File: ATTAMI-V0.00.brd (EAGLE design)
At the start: 22.8 x 22.9 mm, 24 parts, among them U1 MIC5225, U2 ATTINY85-20SU

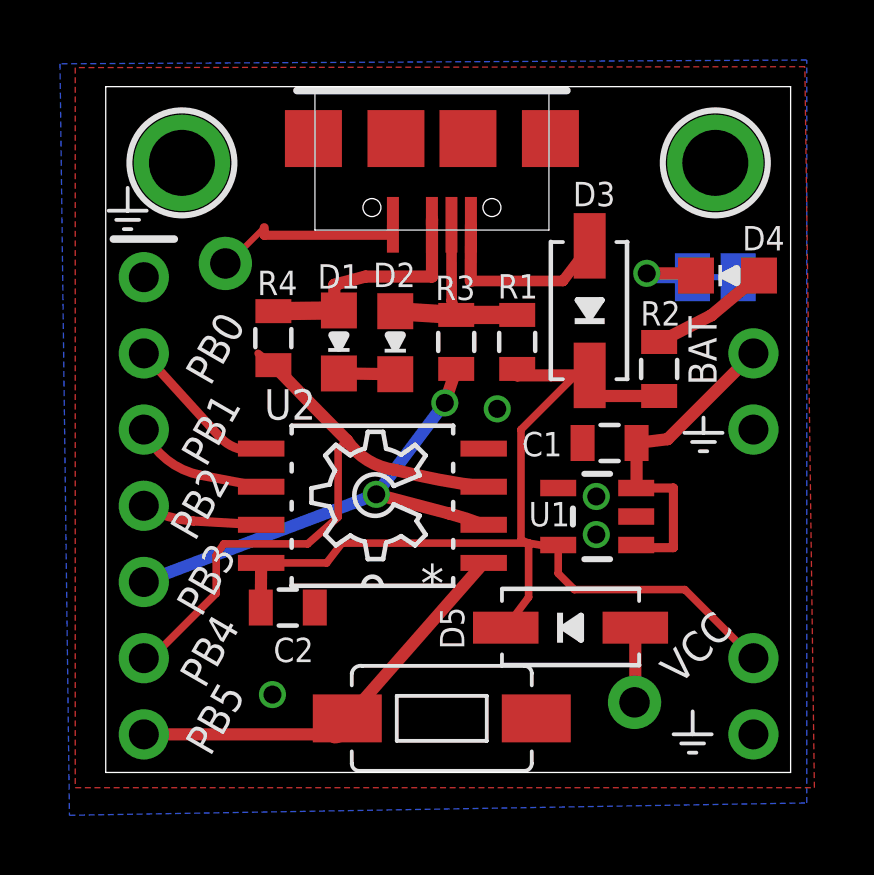
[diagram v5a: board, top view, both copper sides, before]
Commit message: changes in trace width (8mil) and fine tune the aliexpress microusb packge
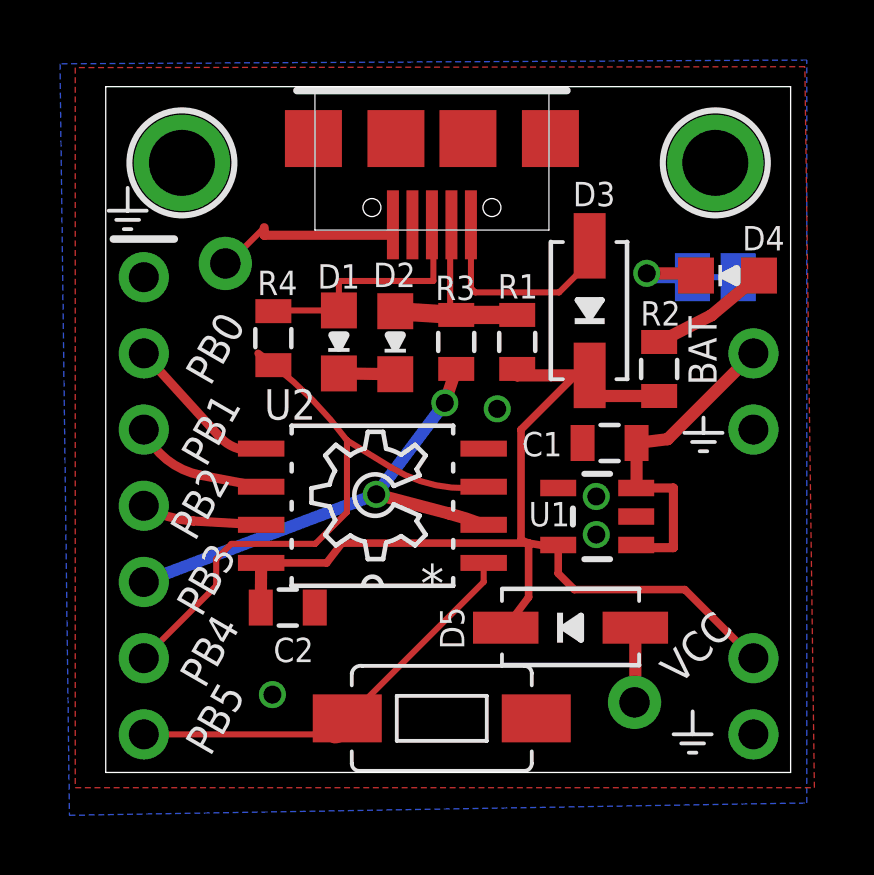
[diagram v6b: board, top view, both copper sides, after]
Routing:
- net V-BUS: track 6.60 -> 7.26 mm
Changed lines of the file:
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@@
 <wire x1="11.684" y1="15.251" x2="13.716" y2="15.251" width="0.6096" layer="1"/>
 <wire x1="11.523740625" y1="18.2553" x2="11.557" y2="18.4553" width="0.3048" layer="1"/>
-<wire x1="11.684" y1="15.251" x2="11.5316" y2="15.7226" width="0.3556" layer="1"/>
-<wire x1="11.5316" y1="15.7226" x2="11.523740625" y2="18.2553" width="0.3556" layer="1"/>
+<wire x1="11.523740625" y1="18.2553" x2="11.4808" y2="18.2553" width="0.2032" layer="1"/>
+<wire x1="11.4808" y1="18.2553" x2="11.4808" y2="15.4542" width="0.2032" layer="1"/>
+<wire x1="11.4808" y1="15.4542" x2="11.684" y2="15.251" width="0.2032" layer="1"/>
 </signal>
 <signal name="GND">
@@
 <contactref element="R4" pad="2"/>
 <wire x1="5.08" y1="13.97" x2="5.588" y2="13.578" width="0.254" layer="1"/>
-<wire x1="8.041640625" y1="11.06931875" x2="5.588" y2="13.578" width="0.4064" layer="1" curve="-1.045178"/>
-<wire x1="8.041640625" y1="11.06931875" x2="9.652" y2="10.0838" width="0.4064" layer="1" curve="48.784139"/>
 <contactref element="J1" pad="6"/>
 <contactref element="U2" pad="3"/>
-<wire x1="9.652" y1="10.0838" x2="12.5984" y2="9.525" width="0.4064" layer="1" curve="7.241306"/>
 <wire x1="1.27" y1="3.81" x2="1.524" y2="3.81" width="0.254" layer="1"/>
-<wire x1="1.524" y1="3.81" x2="3.683" y2="5.969" width="0.254" layer="1"/>
-<wire x1="3.683" y1="5.969" x2="3.683" y2="7.239" width="0.254" layer="1"/>
-<wire x1="3.683" y1="7.239" x2="3.937" y2="7.62" width="0.254" layer="1"/>
-<wire x1="3.937" y1="7.62" x2="6.731" y2="7.62" width="0.254" layer="1"/>
-<wire x1="6.731" y1="7.62" x2="7.747" y2="8.509" width="0.254" layer="1"/>
-<wire x1="7.747" y1="8.509" x2="7.747" y2="10.774678125" width="0.254" layer="1"/>
-<wire x1="7.747" y1="10.774678125" x2="8.041640625" y2="11.06931875" width="0.254" layer="1"/>
+<wire x1="5.588" y1="13.578" x2="8.041640625" y2="11.06931875" width="0.2032" layer="1" curve="-15.959573"/>
+<wire x1="8.041640625" y1="11.06931875" x2="9.525" y2="10.16" width="0.2032" layer="1"/>
+<wire x1="9.525" y1="10.16" x2="12.5984" y2="9.525" width="0.2032" layer="1" curve="39.670268"/>
+<wire x1="8.041640625" y1="11.06931875" x2="8.041640625" y2="8.676640625" width="0.2032" layer="1"/>
+<wire x1="8.041640625" y1="8.676640625" x2="6.985" y2="7.62" width="0.2032" layer="1"/>
+<wire x1="6.985" y1="7.62" x2="4.191" y2="7.62" width="0.2032" layer="1"/>
+<wire x1="4.191" y1="7.62" x2="3.683" y2="7.112" width="0.2032" layer="1"/>
+<wire x1="3.683" y1="7.112" x2="3.683" y2="6.223" width="0.2032" layer="1"/>
+<wire x1="3.683" y1="6.223" x2="1.27" y2="3.81" width="0.2032" layer="1"/>
 </signal>
 <signal name="PB5">
@@
 <wire x1="8.0514" y1="1.8034" x2="7.645" y2="1.27" width="0.6096" layer="1" curve="-90"/>
 <contactref element="J1" pad="7"/>
-<wire x1="1.27" y1="1.27" x2="7.645" y2="1.27" width="0.4064" layer="1"/>
 <contactref element="U2" pad="1"/>
-<wire x1="12.5984" y1="6.985" x2="8.0514" y2="1.8034" width="0.4064" layer="1"/>
+<wire x1="12.5984" y1="6.985" x2="12.5984" y2="6.3504" width="0.2032" layer="1"/>
+<wire x1="12.5984" y1="6.3504" x2="8.0514" y2="1.8034" width="0.2032" layer="1"/>
+<wire x1="7.645" y1="1.27" x2="1.27" y2="1.27" width="0.2032" layer="1"/>
 </signal>
 <signal name="V_BAT">
@@
 <contactref element="D1" pad="A"/>
 <contactref element="USB" pad="DP"/>
-<wire x1="5.588" y1="15.378" x2="7.7724" y2="15.401" width="0.6096" layer="1"/>
-<wire x1="10.873740625" y1="18.2553" x2="10.87628125" y2="18.4553" width="0.4064" layer="1"/>
-<wire x1="10.87628125" y1="18.4553" x2="10.87628125" y2="16.53031875" width="0.4064" layer="1"/>
-<wire x1="10.87628125" y1="16.53031875" x2="8.65631875" y2="16.53031875" width="0.4064" layer="1"/>
-<wire x1="8.65631875" y1="16.53031875" x2="7.62" y2="16.256" width="0.4064" layer="1"/>
-<wire x1="7.62" y1="16.256" x2="7.62" y2="15.5534" width="0.4064" layer="1"/>
-<wire x1="7.62" y1="15.5534" x2="7.7724" y2="15.401" width="0.4064" layer="1"/>
+<wire x1="10.873740625" y1="18.2553" x2="10.922" y2="18.2553" width="0.2032" layer="1"/>
+<wire x1="10.922" y1="18.2553" x2="10.922" y2="16.383" width="0.2032" layer="1"/>
+<wire x1="10.922" y1="16.383" x2="7.7724" y2="16.383" width="0.2032" layer="1"/>
+<wire x1="7.7724" y1="16.383" x2="7.7724" y2="15.401" width="0.2032" layer="1"/>
+<wire x1="7.7724" y1="15.401" x2="5.611" y2="15.401" width="0.2032" layer="1"/>
+<wire x1="5.611" y1="15.401" x2="5.588" y2="15.378" width="0.2032" layer="1"/>
 </signal>
 <signal name="VCC">
@@
 <contactref element="USB" pad="VCC"/>
 <contactref element="D3" pad="AQ"/>
-<wire x1="12.173740625" y1="18.2553" x2="12.1666" y2="16.383" width="0.4064" layer="1"/>
 <wire x1="16.0274" y1="17.7038" x2="16.1315375" y2="17.553940625" width="0.4064" layer="1" curve="-7.449454"/>
-<wire x1="12.1666" y1="16.383" x2="15.24" y2="16.383" width="0.3556" layer="1"/>
-<wire x1="15.24" y1="16.383" x2="16.1315375" y2="17.553940625" width="0.3556" layer="1"/>
+<wire x1="12.173740625" y1="18.2553" x2="12.173740625" y2="16.147259375" width="0.2032" layer="1"/>
+<wire x1="12.173740625" y1="16.147259375" x2="12.319" y2="16.002" width="0.2032" layer="1"/>
+<wire x1="12.319" y1="16.002" x2="15.113" y2="16.002" width="0.2032" layer="1"/>
+<wire x1="15.113" y1="16.002" x2="16.002" y2="16.891" width="0.2032" layer="1"/>
+<wire x1="16.002" y1="16.891" x2="16.002" y2="17.424403125" width="0.2032" layer="1"/>
+<wire x1="16.002" y1="17.424403125" x2="16.1315375" y2="17.553940625" width="0.2032" layer="1"/>
 </signal>
 <signal name="N$2">

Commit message: new design with added AMS1117 voltage regulator
with library reflecting the part
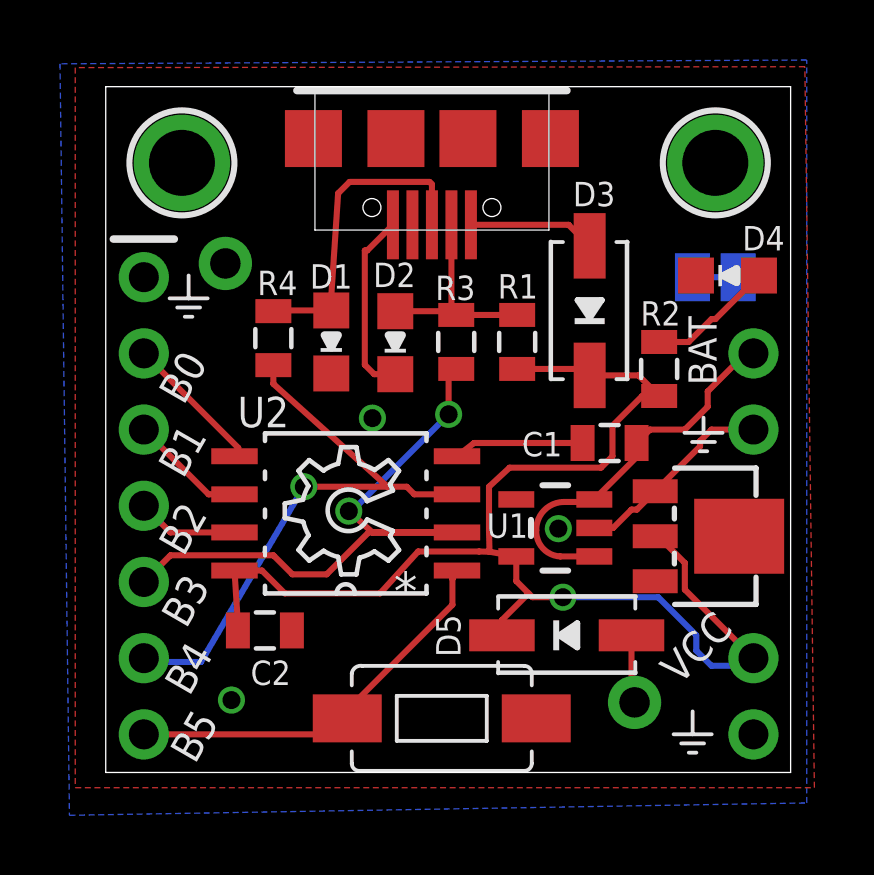
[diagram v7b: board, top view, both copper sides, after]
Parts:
- added 1117: (no value), ATtami:SOT89
- moved U1 1.45 mm to (15.0, 8.15)
- moved C2 1.08 mm to (5.31, 4.73)
- moved U$3 1.02 mm to (9.78, 6.60)
- moved U2 0.92 mm to (8.00, 8.64)
- moved D5 0.28 mm to (15.4, 4.57)
- moved D1 0.25 mm to (7.52, 14.4)
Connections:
- net GND: now also 1117.1
- net VCC: now also 1117.2
- net V_BAT: now also 1117.3
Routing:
- net GND: track 8.55 -> 17.4 mm, vias 4 -> 3
- net VCC: track 36.1 -> 44.7 mm, vias 0 -> 1
- net PB3: track 17.0 -> 21.8 mm
- net N$7: track 8.25 -> 11.5 mm
- net N$13: track 3.24 -> 0.00 mm, vias 1 -> 0
- net V-BUS: track 7.26 -> 4.25 mm
- net V_BAT: track 11.3 -> 12.6 mm
- net PB4: track 21.0 -> 19.7 mm, vias 0 -> 1
- net PB5: track 14.1 -> 13.4 mm
- net PB2: track 3.99 -> 3.39 mm
- net PB1: track 4.48 -> 3.92 mm
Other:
- board text added: "B0"
- board text added: "B1"
- board text added: "B2"
- board text added: "B3"
- board text added: "B4"
- board text added: "B5"

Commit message: layout fixing and pdf
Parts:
- moved D5 0.40 mm to (15.0, 4.70)
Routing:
- net GND: track 17.4 -> 14.8 mm
- net V_BAT: track 12.6 -> 14.8 mm
- net VCC: track 44.7 -> 44.1 mm
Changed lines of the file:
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@@
 </element>
 <element name="C2" library="ATtami" package="0805" value="2.2uf/16V" x="5.306059375" y="4.734559375" smashed="yes">
-<attribute name="NAME" x="4.828540625" y="2.91591875" size="0.8128" layer="25"/>
+<attribute name="NAME" x="5.463540625" y="3.04291875" size="0.8128" layer="25"/>
 </element>
 <element name="D1" library="ATtami" package="LED-805" value="Blue LED" x="7.5184" y="14.351" smashed="yes" rot="R180">
@@
 <attribute name="VALUE" x="-1.905" y="17.78" size="0.4064" layer="27" ratio="10" rot="R270"/>
 </element>
-<element name="D5" library="ATtami" package="SOD-323" value="Schottky" x="15.367" y="4.572" smashed="yes">
-<attribute name="NAME" x="11.827" y="3.853" size="0.8128" layer="25" font="vector" ratio="18" rot="R90"/>
-<attribute name="VALUE" x="13.124" y="2.526" size="0.4064" layer="27" ratio="10" display="off"/>
+<element name="D5" library="ATtami" package="SOD-323" value="Schottky" x="14.986" y="4.699" smashed="yes">
+<attribute name="NAME" x="11.446" y="3.98" size="0.8128" layer="25" font="vector" ratio="18" rot="R90"/>
+<attribute name="VALUE" x="12.743" y="2.653" size="0.4064" layer="27" ratio="10" display="off"/>
 </element>
 <element name="SJ1" library="ATtami" package="SOLDERJUMPER_CLOSEDWIRE" value="" x="20.32" y="16.51" smashed="yes" rot="MR0">
@@
 <wire x1="12.277459375" y1="10.982059375" x2="11.7094" y2="10.541" width="0.2032" layer="1"/>
 <via x="15.0876" y="8.128" extent="1-16" drill="0.6"/>
-<wire x1="16.286103125" y1="8.1508625" x2="16.9138625" y2="8.1508625" width="0.2032" layer="1"/>
-<wire x1="16.9138625" y1="8.1508625" x2="17.526" y2="8.763" width="0.2032" layer="1"/>
-<wire x1="17.526" y1="8.763" x2="17.705" y2="8.763" width="0.2032" layer="1"/>
-<wire x1="17.705" y1="8.763" x2="18.316" y2="9.374" width="0.2032" layer="1"/>
 <wire x1="21.59" y1="11.43" x2="20.193" y2="11.43" width="0.2032" layer="1"/>
 <wire x1="20.193" y1="11.43" x2="19.812" y2="11.049" width="0.2032" layer="1"/>
@@
 <wire x1="8.9494" y1="13.2756" x2="8.636" y2="13.589" width="0.2032" layer="1"/>
 <wire x1="8.636" y1="13.589" x2="8.636" y2="17.399" width="0.2032" layer="1"/>
-<wire x1="8.636" y1="17.399" x2="8.717440625" y2="17.399" width="0.2032" layer="1"/>
-<wire x1="8.717440625" y1="17.399" x2="9.573740625" y2="18.2553" width="0.2032" layer="1"/>
+<wire x1="8.636" y1="17.399" x2="8.717440625" y2="17.526" width="0.2032" layer="1"/>
+<wire x1="8.717440625" y1="17.526" x2="9.573740625" y2="18.2553" width="0.2032" layer="1"/>
 <via x="8.89" y="11.811" extent="1-16" drill="0.6"/>
 <via x="4.191" y="2.413" extent="1-16" drill="0.6"/>
@@
 <wire x1="8.763" y1="8.001" x2="7.366" y2="6.604" width="0.2032" layer="1"/>
 <wire x1="7.366" y1="6.604" x2="6.223" y2="6.604" width="0.2032" layer="1"/>
-<wire x1="6.223" y1="6.604" x2="5.588" y2="7.239" width="0.2032" layer="1"/>
-<wire x1="5.588" y1="7.239" x2="2.159" y2="7.239" width="0.2032" layer="1"/>
-<wire x1="2.159" y1="7.239" x2="1.27" y2="6.35" width="0.2032" layer="1"/>
+<wire x1="6.223" y1="6.604" x2="5.588" y2="7.366" width="0.2032" layer="1"/>
+<wire x1="5.588" y1="7.366" x2="2.159" y2="7.366" width="0.2032" layer="1"/>
+<wire x1="2.159" y1="7.366" x2="1.27" y2="6.35" width="0.2032" layer="1"/>
 <wire x1="11.7094" y1="8.001" x2="8.89" y2="8.001" width="0.2032" layer="1"/>
 <wire x1="8.89" y1="8.001" x2="8.1026" y2="8.7122" width="0.2032" layer="1"/>
@@
 <wire x1="15.2654" y1="9.017" x2="16.202240625" y2="9.017" width="0.2032" layer="1"/>
 <wire x1="16.202240625" y1="9.017" x2="16.286103125" y2="9.1008625" width="0.2032" layer="1" curve="90"/>
-<wire x1="16.286103125" y1="7.2008625" x2="18.316" y2="6.374" width="0" layer="19" extent="1-1"/>
+<wire x1="16.286103125" y1="7.2008625" x2="18.316" y2="6.374" width="0.254" layer="1"/>
 </signal>
 <signal name="N$7">
@@
 <wire x1="10.873740625" y1="19.606259375" x2="10.795" y2="19.685" width="0.2032" layer="1"/>
 <wire x1="10.795" y1="19.685" x2="8.128" y2="19.685" width="0.2032" layer="1"/>
-<wire x1="8.128" y1="19.685" x2="7.747" y2="19.304" width="0.2032" layer="1"/>
-<wire x1="7.747" y1="19.304" x2="7.493" y2="15.494" width="0.2032" layer="1"/>
+<wire x1="8.128" y1="19.685" x2="7.493" y2="19.177" width="0.2032" layer="1"/>
+<wire x1="7.493" y1="19.177" x2="7.493" y2="15.494" width="0.2032" layer="1"/>
 <wire x1="7.493" y1="15.494" x2="7.112" y2="15.113" width="0.2032" layer="1"/>
 <wire x1="7.112" y1="15.113" x2="7.2304" y2="15.113" width="0.2032" layer="1"/>
@@
 <wire x1="17.8833" y1="12.5493" x2="16.891" y2="11.557" width="0.2032" layer="1"/>
 <wire x1="16.891" y1="11.557" x2="16.891" y2="10.541" width="0.2032" layer="1"/>
-<wire x1="16.891" y1="10.541" x2="16.51" y2="10.16" width="0.2032" layer="1"/>
-<wire x1="16.51" y1="10.16" x2="13.462" y2="10.16" width="0.2032" layer="1"/>
-<wire x1="13.462" y1="10.16" x2="12.7762" y2="9.525" width="0.2032" layer="1"/>
+<wire x1="16.891" y1="10.541" x2="16.383" y2="9.906" width="0.2032" layer="1"/>
+<wire x1="16.383" y1="9.906" x2="13.335" y2="9.906" width="0.2032" layer="1"/>
+<wire x1="13.335" y1="9.906" x2="12.7762" y2="9.525" width="0.2032" layer="1"/>
 <wire x1="12.7762" y1="9.525" x2="12.7762" y2="8.059765625" width="0.2032" layer="1"/>
 <wire x1="12.7762" y1="8.059765625" x2="12.792884375" y2="7.35728125" width="0.2032" layer="1"/>
 <wire x1="12.792884375" y1="7.35728125" x2="13.685903125" y2="7.2008625" width="0.2032" layer="1"/>
-<wire x1="4.2926" y1="6.731" x2="4.4196" y2="4.7481" width="0.2032" layer="1"/>
-<wire x1="4.4196" y1="4.7481" x2="4.406059375" y2="4.734559375" width="0.2032" layer="1"/>
 <wire x1="4.2926" y1="6.731" x2="5.207" y2="6.731" width="0.2032" layer="1"/>
-<wire x1="5.207" y1="6.731" x2="5.969" y2="5.969" width="0.2032" layer="1"/>
-<wire x1="5.969" y1="5.969" x2="9.144" y2="5.969" width="0.2032" layer="1"/>
-<wire x1="9.144" y1="5.969" x2="10.414" y2="7.366" width="0.2032" layer="1"/>
+<wire x1="5.207" y1="6.731" x2="6.096" y2="6.096" width="0.2032" layer="1"/>
+<wire x1="6.096" y1="6.096" x2="9.271" y2="6.096" width="0.2032" layer="1"/>
+<wire x1="9.271" y1="6.096" x2="10.414" y2="7.366" width="0.2032" layer="1"/>
 <wire x1="10.414" y1="7.366" x2="12.446003125" y2="7.366" width="0.2032" layer="1"/>
 <wire x1="12.446003125" y1="7.366" x2="12.792884375" y2="7.35728125" width="0.2032" layer="1"/>
@@
 <via x="15.24" y="5.842" extent="1-16" drill="0.6"/>
 <wire x1="15.24" y1="5.842" x2="18.415" y2="5.842" width="0.2032" layer="16"/>
-<wire x1="18.415" y1="5.842" x2="19.685" y2="4.572" width="0.2032" layer="16"/>
-<wire x1="19.685" y1="4.572" x2="19.685" y2="4.064" width="0.2032" layer="16"/>
-<wire x1="19.685" y1="4.064" x2="20.193" y2="3.556" width="0.2032" layer="16"/>
-<wire x1="20.193" y1="3.556" x2="21.336" y2="3.556" width="0.2032" layer="16"/>
-<wire x1="21.336" y1="3.556" x2="21.59" y2="3.81" width="0.2032" layer="16"/>
-<wire x1="13.208" y1="4.572" x2="13.208" y2="5.08" width="0.2032" layer="1"/>
-<wire x1="13.208" y1="5.08" x2="14.097" y2="5.969" width="0.2032" layer="1"/>
+<wire x1="12.827" y1="4.699" x2="14.097" y2="5.969" width="0.2032" layer="1"/>
+<wire x1="4.2926" y1="6.731" x2="4.406059375" y2="6.617540625" width="0.254" layer="1"/>
+<wire x1="4.406059375" y1="6.617540625" x2="4.406059375" y2="4.734559375" width="0.254" layer="1"/>
+<wire x1="18.415" y1="5.842" x2="19.558" y2="5.842" width="0.254" layer="16"/>
+<wire x1="19.558" y1="5.842" x2="21.59" y2="3.81" width="0.254" layer="16"/>
 </signal>
 <signal name="PB1">
@@
 <contactref element="D5" pad="AQ"/>
 <contactref element="COIN_CELL_(+)" pad="1"/>
-<wire x1="17.526" y1="4.572" x2="17.526" y2="2.4384" width="0.2032" layer="1"/>
+<wire x1="17.145" y1="4.699" x2="17.526" y2="2.4384" width="0.2032" layer="1"/>
 <wire x1="17.526" y1="2.4384" x2="17.6276" y2="2.3368" width="0.2032" layer="1"/>
 </signal>
